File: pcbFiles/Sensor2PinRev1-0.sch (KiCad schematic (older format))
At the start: 2 parts

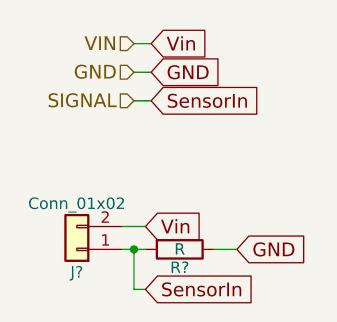
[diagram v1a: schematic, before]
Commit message: Update Footprints and Board Layers
Still need to get foorprint for x... device and the lpf may need to make them if I cannot find them @willcarroll7
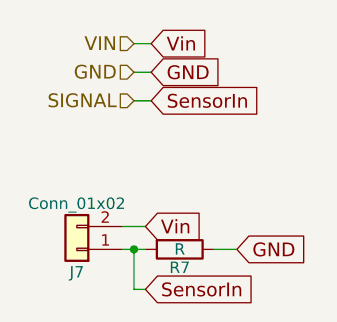
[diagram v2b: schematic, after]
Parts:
- J7: renamed from J?; footprint (none) -> Pin_Headers:Pin_Header_Straight_1x02_Pitch2.54mm
- R7: renamed from R?; footprint (none) -> Resistors_SMD:R_0402
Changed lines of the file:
@@
-EESchema Schematic File Version 4
+EESchema Schematic File Version 2
 LIBS:power
+LIBS:device
+LIBS:switches
+LIBS:relays
+LIBS:motors
+LIBS:transistors
+LIBS:conn
+LIBS:linear
+LIBS:regul
 LIBS:74xx
+LIBS:cmos4000
+LIBS:adc-dac
+LIBS:memory
+LIBS:xilinx
+LIBS:microcontrollers
+LIBS:dsp
+LIBS:microchip
+LIBS:analog_switches
+LIBS:motorola
+LIBS:texas
+LIBS:intel
+LIBS:audio
+LIBS:interface
+LIBS:digital-audio
+LIBS:philips
+LIBS:display
+LIBS:cypress
+LIBS:siliconi
+LIBS:opto
+LIBS:atmel
+LIBS:contrib
+LIBS:valves
+LIBS:ADS1115IDGST
+LIBS:CYW20719B1KUMLG
+LIBS:LSM9DS1TR
+LIBS:TPS63001DRCT
+LIBS:MCP73831T-2ACI_OT
+LIBS:A-1JB
+LIBS:XC6119N16A7R-G
 LIBS:GolfGloveMainBoardV1.0.0-cache
-EELAYER 26 0
+EELAYER 25 0
 EELAYER END
 $Descr A4 11693 8268
 encoding utf-8
-Sheet 7 12
+Sheet 12 12
 Title ""
 Date ""
@@
 $EndDescr
 $Comp
-L R R?
+L R R7
 U 1 1 5C4B94B6
 P 5150 3175
-AR Path="/5C4B9358/5C4B94B6" Ref="R?"  Part="1"
-AR Path="/5C4BB400/5C4B94B6" Ref="R?"  Part="1"
-AR Path="/5C4BB725/5C4B94B6" Ref="R?"  Part="1"
-AR Path="/5C4BB72A/5C4B94B6" Ref="R?"  Part="1"
-AR Path="/5C4BBBA5/5C4B94B6" Ref="R?"  Part="1"
-AR Path="/5C4BBBAA/5C4B94B6" Ref="R?"  Part="1"
-F 0 "R?" V 5230 3175 50  0000 C CNN
+AR Path="/5C4B9358/5C4B94B6" Ref="R7"  Part="1"
+AR Path="/5C4BB400/5C4B94B6" Ref="R8"  Part="1"
+AR Path="/5C4BB725/5C4B94B6" Ref="R9"  Part="1"
+AR Path="/5C4BB72A/5C4B94B6" Ref="R10"  Part="1"
+AR Path="/5C4BBBA5/5C4B94B6" Ref="R12"  Part="1"
+AR Path="/5C4BBBAA/5C4B94B6" Ref="R13"  Part="1"
+F 0 "R7" V 5230 3175 50  0000 C CNN
 F 1 "R" V 5150 3175 50  0000 C CNN
-F 2 "" V 5080 3175 50  0001 C CNN
+F 2 "Resistors_SMD:R_0402" V 5080 3175 50  0001 C CNN
 F 3 "" H 5150 3175 50  0001 C CNN
 	1    5150 3175
@@
 $EndComp
 $Comp
-L Conn_01x02 J?
+L Conn_01x02 J7
 U 1 1 5C4B9547
 P 4700 3175
-AR Path="/5C4B9358/5C4B9547" Ref="J?"  Part="1"
-AR Path="/5C4BB400/5C4B9547" Ref="J?"  Part="1"
-AR Path="/5C4BB725/5C4B9547" Ref="J?"  Part="1"
-AR Path="/5C4BB72A/5C4B9547" Ref="J?"  Part="1"
-AR Path="/5C4BBBA5/5C4B9547" Ref="J?"  Part="1"
-AR Path="/5C4BBBAA/5C4B9547" Ref="J?"  Part="1"
-F 0 "J?" H 4700 3275 50  0000 C CNN
+AR Path="/5C4B9358/5C4B9547" Ref="J7"  Part="1"
+AR Path="/5C4BB400/5C4B9547" Ref="J8"  Part="1"
+AR Path="/5C4BB725/5C4B9547" Ref="J9"  Part="1"
+AR Path="/5C4BB72A/5C4B9547" Ref="J14"  Part="1"
+AR Path="/5C4BBBA5/5C4B9547" Ref="J15"  Part="1"
+AR Path="/5C4BBBAA/5C4B9547" Ref="J16"  Part="1"
+F 0 "J7" H 4700 3275 50  0000 C CNN
 F 1 "Conn_01x02" H 4700 2975 50  0000 C CNN
-F 2 "" H 4700 3175 50  0001 C CNN
+F 2 "Pin_Headers:Pin_Header_Straight_1x02_Pitch2.54mm" H 4700 3175 50  0001 C CNN
 F 3 "" H 4700 3175 50  0001 C CNN
 	1    4700 3175

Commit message: Add Pin Header For 5v UART Connection
Added a 1x2 2.54mm Pitch pin header for the 5v UART line. This line feeds directly into the pin of the buck converter and therefore we will need to be sure to NOT turn on the device when programming or when this jumper is connected. @willcarroll7
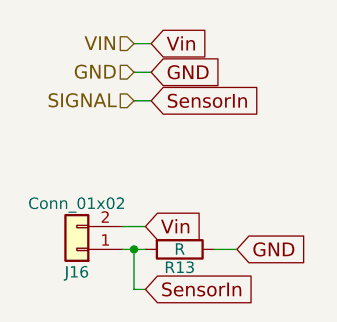
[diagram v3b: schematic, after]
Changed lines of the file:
@@
 LIBS:contrib
 LIBS:valves
-LIBS:ADS1115IDGST
-LIBS:CYW20719B1KUMLG
-LIBS:LSM9DS1TR
-LIBS:TPS63001DRCT
-LIBS:MCP73831T-2ACI_OT
-LIBS:A-1JB
-LIBS:XC6119N16A7R-G
 LIBS:GolfGloveMainBoardV1.0.0-cache
 EELAYER 25 0
@@
 AR Path="/5C4BBBA5/5C4B94B6" Ref="R12"  Part="1"
 AR Path="/5C4BBBAA/5C4B94B6" Ref="R13"  Part="1"
-F 0 "R7" V 5230 3175 50  0000 C CNN
+F 0 "R13" V 5230 3175 50  0000 C CNN
 F 1 "R" V 5150 3175 50  0000 C CNN
 F 2 "Resistors_SMD:R_0402" V 5080 3175 50  0001 C CNN
@@
 AR Path="/5C4BBBA5/5C4B9547" Ref="J15"  Part="1"
 AR Path="/5C4BBBAA/5C4B9547" Ref="J16"  Part="1"
-F 0 "J7" H 4700 3275 50  0000 C CNN
+F 0 "J16" H 4700 3275 50  0000 C CNN
 F 1 "Conn_01x02" H 4700 2975 50  0000 C CNN
 F 2 "Pin_Headers:Pin_Header_Straight_1x02_Pitch2.54mm" H 4700 3175 50  0001 C CNN

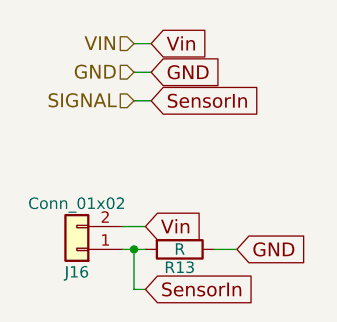
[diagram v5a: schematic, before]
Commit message: Update Board Files
Updated schematic files, completed REV1.0 of the board design, waiting for review by @willcarroll7
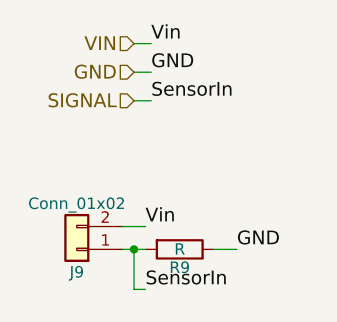
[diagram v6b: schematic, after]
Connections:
- net SensorIn renamed SIGNAL
- net Vin renamed VIN
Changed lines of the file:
@@
 LIBS:contrib
 LIBS:valves
-LIBS:2450AT42B100E
-LIBS:A-1JB
 LIBS:ADS1115IDGST
-LIBS:CD4011BM96
 LIBS:CYW20719B1KUMLG
 LIBS:LSM9DS1TR
+LIBS:TPS63001DRCT
 LIBS:MCP73831T-2ACI_OT
+LIBS:A-1JB
+LIBS:XC6119N16A7R-G
+LIBS:2450AT42B100E
+LIBS:CD4011BM96
 LIBS:MMDT3904V-7
 LIBS:MMPQ3904
 LIBS:S2B-PH-K-S_LF__SN_
-LIBS:TPS63001DRCT
-LIBS:XC6119N16A7R-G
 LIBS:GolfGloveMainBoardV1.0.0-cache
 EELAYER 25 0
@@
 $Descr A4 11693 8268
 encoding utf-8
-Sheet 12 12
+Sheet 9 12
 Title ""
 Date ""
@@
 AR Path="/5C4BBBA5/5C4B94B6" Ref="R12"  Part="1"
 AR Path="/5C4BBBAA/5C4B94B6" Ref="R13"  Part="1"
-F 0 "R13" V 5230 3175 50  0000 C CNN
+F 0 "R9" V 5230 3175 50  0000 C CNN
 F 1 "R" V 5150 3175 50  0000 C CNN
 F 2 "Resistors_SMD:R_0402" V 5080 3175 50  0001 C CNN
@@
 AR Path="/5C4BBBA5/5C4B9547" Ref="J15"  Part="1"
 AR Path="/5C4BBBAA/5C4B9547" Ref="J16"  Part="1"
-F 0 "J16" H 4700 3275 50  0000 C CNN
+F 0 "J9" H 4700 3275 50  0000 C CNN
 F 1 "Conn_01x02" H 4700 2975 50  0000 C CNN
 F 2 "Pin_Headers:Pin_Header_Straight_1x02_Pitch2.54mm" H 4700 3175 50  0001 C CNN
@@
 	-1   0    0    1
 $EndComp
-Text GLabel 5000 3075 2    60   Input ~ 0
-Vin
-Text GLabel 5400 3175 2    60   Input ~ 0
-GND
-Text GLabel 5000 3350 2    60   Input ~ 0
-SensorIn
 Wire Wire Line
 	4900 3075 5000 3075
@@
 Text HLabel 4950 2525 0    60   Input ~ 0
 SIGNAL
-Text GLabel 5025 2275 2    60   Input ~ 0
-Vin
-Text GLabel 5025 2400 2    60   Input ~ 0
-GND
-Text GLabel 5025 2525 2    60   Input ~ 0
-SensorIn
 Wire Wire Line
 	4950 2275 5025 2275
@@
 Wire Wire Line
 	4950 2525 5025 2525
+Text Label 5025 2525 0    60   ~ 0
+SensorIn
+Text Label 5025 2400 0    60   ~ 0
+GND
+Text Label 5025 2275 0    60   ~ 0
+Vin
+Text Label 5000 3075 0    60   ~ 0
+Vin
+Text Label 5400 3175 0    60   ~ 0
+GND
+Text Label 5000 3350 0    60   ~ 0
+SensorIn
 $EndSCHEMATC

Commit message: Updates
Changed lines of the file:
@@
 AR Path="/5C4BBBA5/5C4B94B6" Ref="R12"  Part="1"
 AR Path="/5C4BBBAA/5C4B94B6" Ref="R13"  Part="1"
-F 0 "R9" V 5230 3175 50  0000 C CNN
+F 0 "R13" V 5230 3175 50  0000 C CNN
 F 1 "R" V 5150 3175 50  0000 C CNN
 F 2 "Resistors_SMD:R_0402" V 5080 3175 50  0001 C CNN
@@
 AR Path="/5C4BBBA5/5C4B9547" Ref="J15"  Part="1"
 AR Path="/5C4BBBAA/5C4B9547" Ref="J16"  Part="1"
-F 0 "J9" H 4700 3275 50  0000 C CNN
+F 0 "J16" H 4700 3275 50  0000 C CNN
 F 1 "Conn_01x02" H 4700 2975 50  0000 C CNN
 F 2 "Pin_Headers:Pin_Header_Straight_1x02_Pitch2.54mm" H 4700 3175 50  0001 C CNN
